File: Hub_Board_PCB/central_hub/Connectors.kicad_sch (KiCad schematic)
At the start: 12 parts, among them J3 Screw_Terminal_01x08, J4 Screw_Terminal_01x08, J5 CSP-USC16-TR, J6 Screw_Terminal_01x04, J6 Screw_Terminal_01x06, J8 Conn_01x02

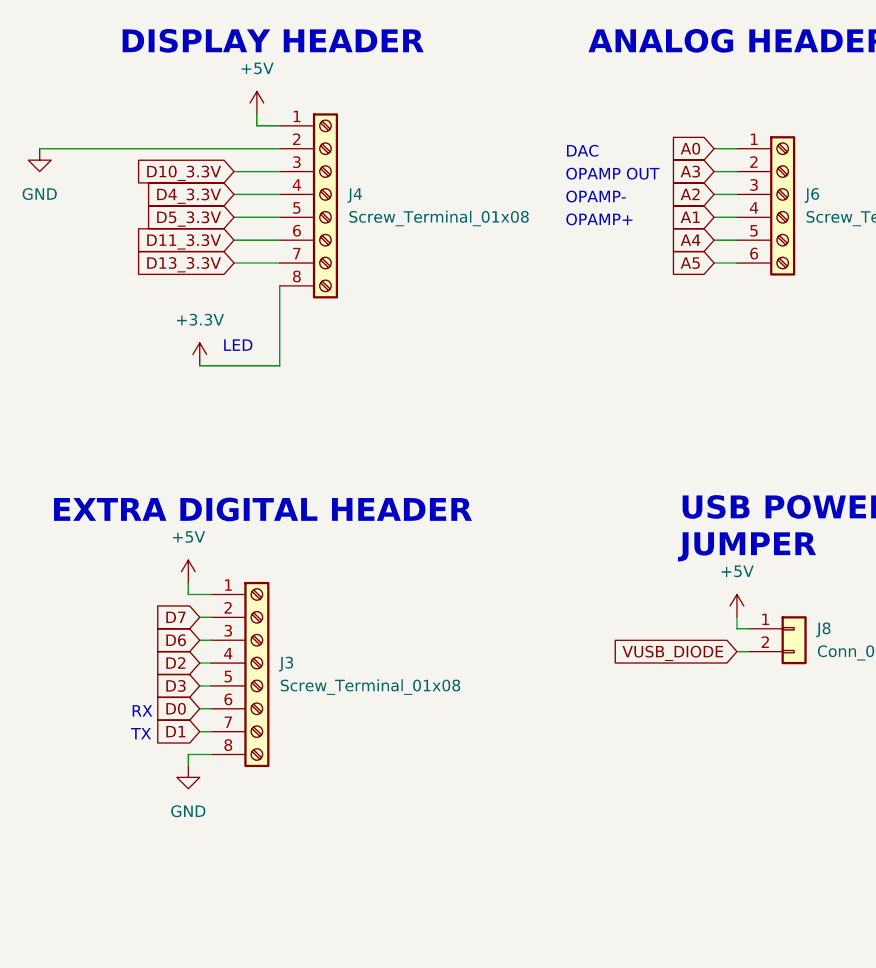
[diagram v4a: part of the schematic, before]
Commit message: Prelim layout + routing for hub PCB
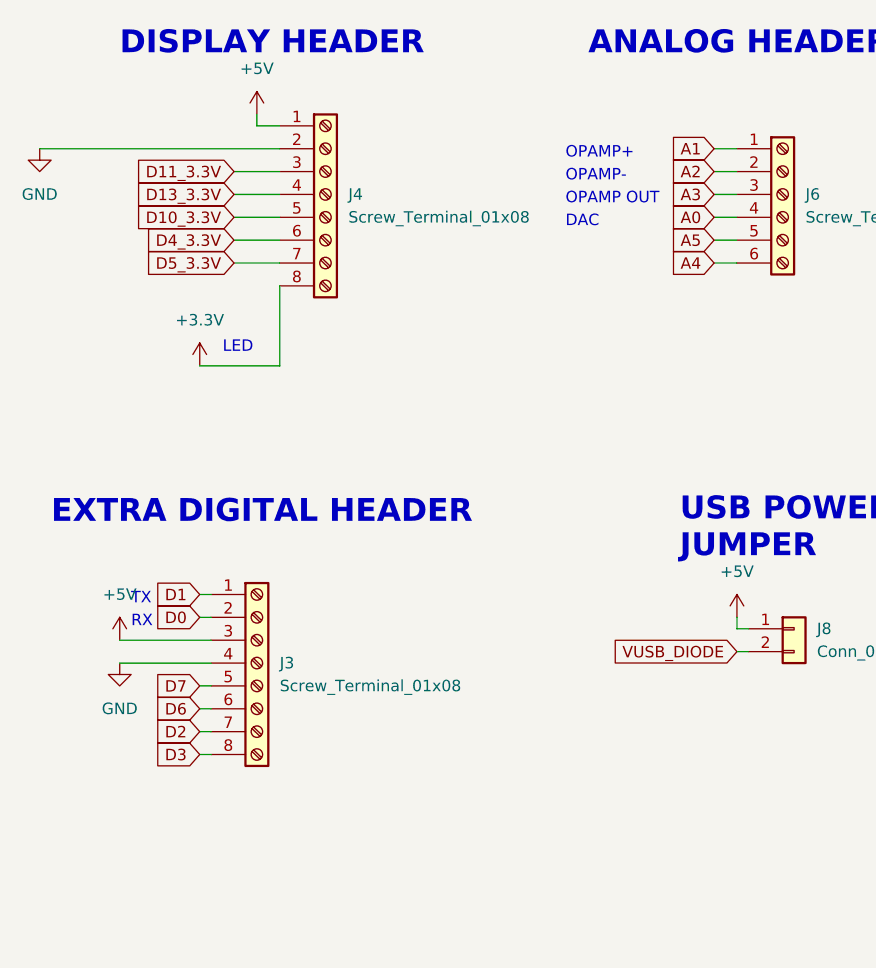
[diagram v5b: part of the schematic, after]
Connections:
- net +5V: now also J3.3 (Pin_3); no longer J3.1 (Pin_1)
- net A0: now also J6.4 (Pin_4); no longer J6.1 (Pin_1)
- net A1: now also J6.1 (Pin_1); no longer J6.4 (Pin_4)
- net A2: now also J6.2 (Pin_2); no longer J6.3 (Pin_3)
- net A3: now also J6.3 (Pin_3); no longer J6.2 (Pin_2)
- net A4: now also J6.6 (Pin_6); no longer J6.5 (Pin_5)
- net A5: now also J6.5 (Pin_5); no longer J6.6 (Pin_6)
- net D0: now also J3.2 (Pin_2); no longer J3.6 (Pin_6)
- net D1: now also J3.1 (Pin_1); no longer J3.7 (Pin_7)
- net D10_3.3V: now also J4.5 (Pin_5); no longer J4.3 (Pin_3)
- net D11_3.3V: now also J4.3 (Pin_3); no longer J4.6 (Pin_6)
- net D13_3.3V: now also J4.4 (Pin_4); no longer J4.7 (Pin_7)
- net D2: now also J3.7 (Pin_7); no longer J3.4 (Pin_4)
- net D3: now also J3.8 (Pin_8); no longer J3.5 (Pin_5)
- net D4_3.3V: now also J4.6 (Pin_6); no longer J4.4 (Pin_4)
- net D5_3.3V: now also J4.7 (Pin_7); no longer J4.5 (Pin_5)
- net D6: now also J3.6 (Pin_6); no longer J3.3 (Pin_3)
- net D7: now also J3.5 (Pin_5); no longer J3.2 (Pin_2)
- net GND: now also J3.4 (Pin_4); no longer J3.8 (Pin_8)

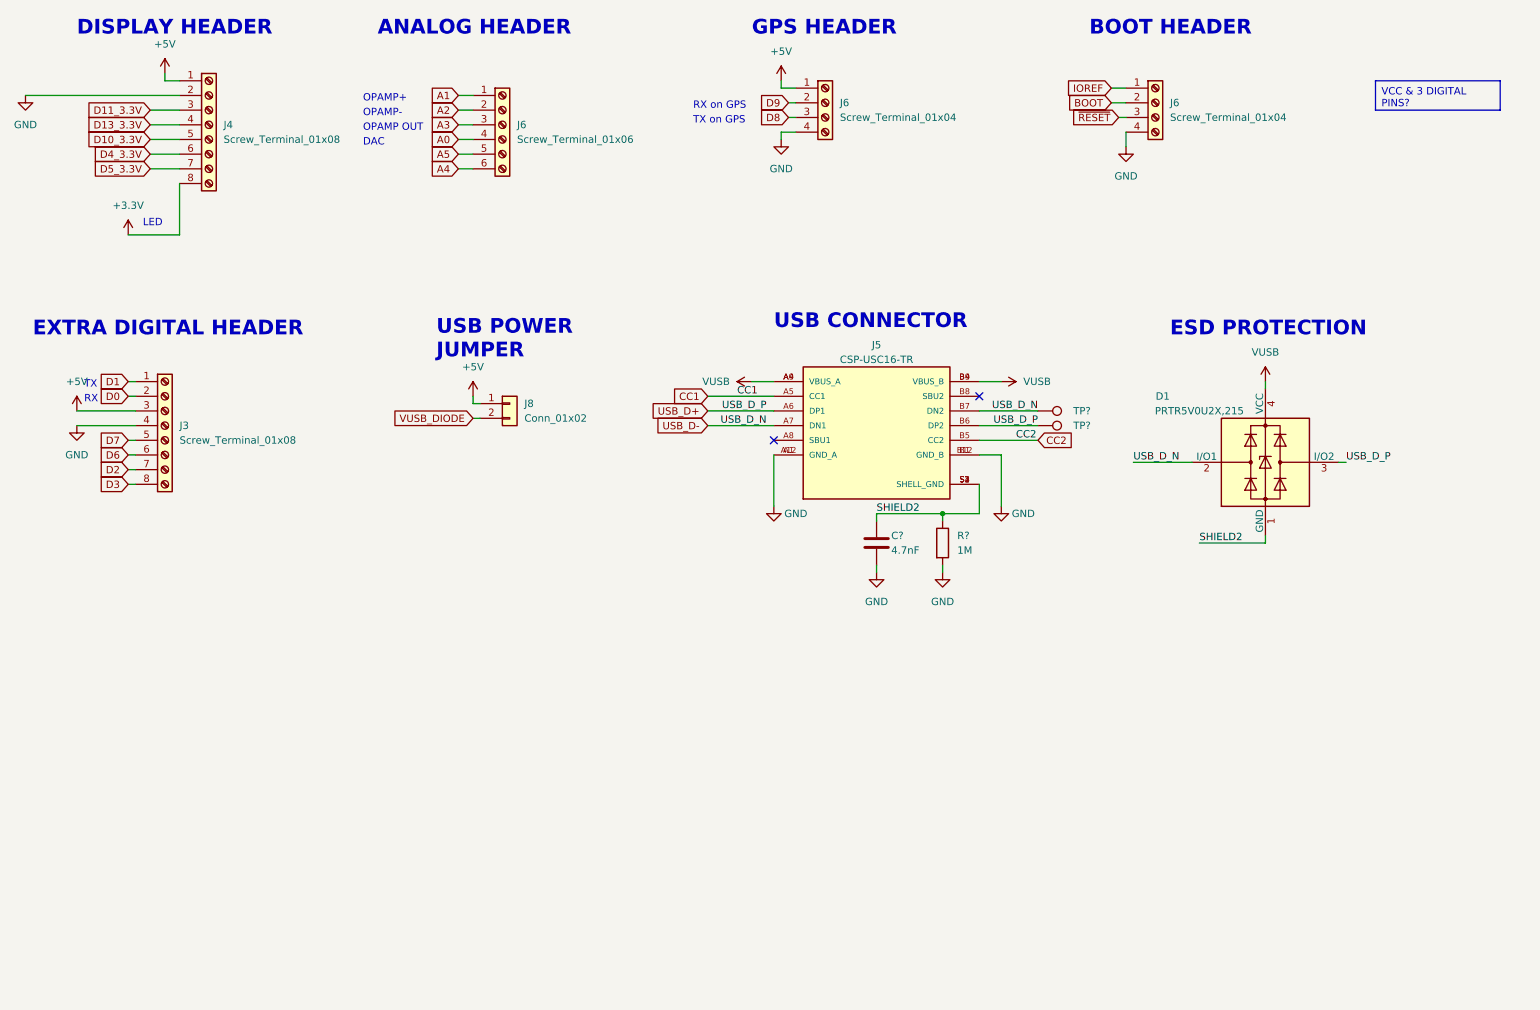
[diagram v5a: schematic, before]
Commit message: - fixed capacitor values on MCU sheet (both central hub and motor board) - added missing Accelerometer componenets - changed BOOT HEADER (both central hub and motor board) - set the Arduino "love" signal to NC - fixed overlapping pins on USB connector
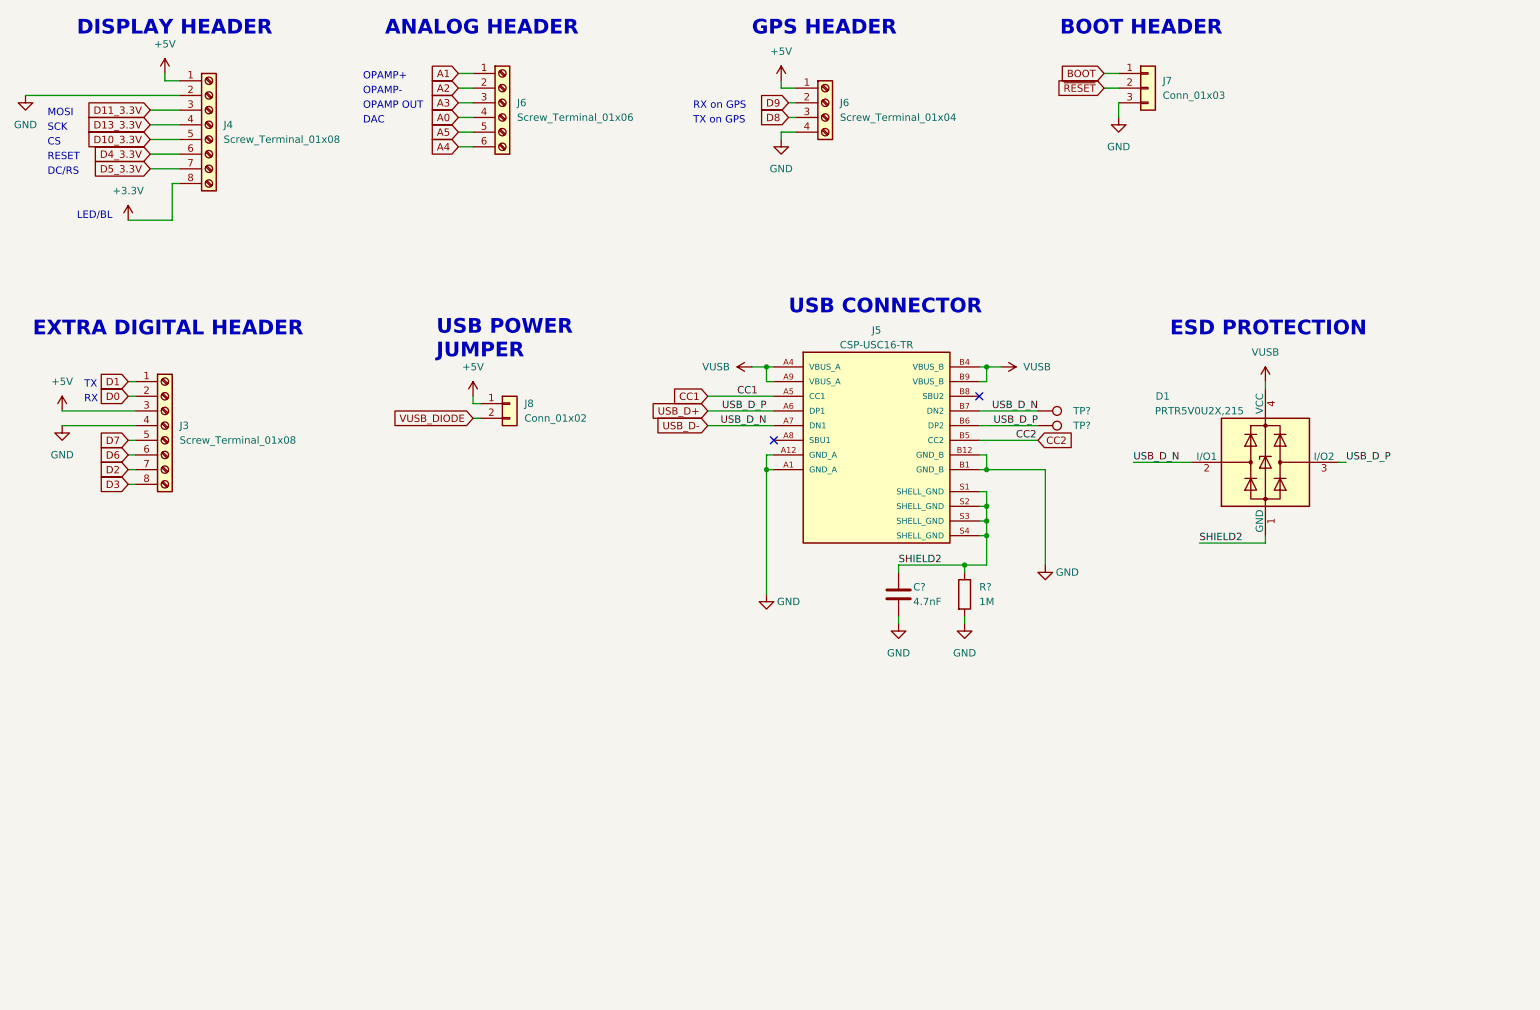
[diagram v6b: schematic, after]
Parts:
- removed J6: Screw_Terminal_01x04, Connector_PinHeader_2.54mm:PinHeader_1x04_P2.54mm_Vertical, symbol Connector:Screw_Terminal_01x04
- added J7: Conn_01x03, Connector_PinHeader_2.54mm:PinHeader_1x03_P2.54mm_Vertical, symbol Connector_Generic:Conn_01x03
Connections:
- net BOOT: now also J7.1 (Pin_1)
- net GND: now also J7.3 (Pin_3)
- net ~{RESET}: now also J7.2 (Pin_2)
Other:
- note added: "CS"
- note added: "DC/RS"
- note added: "LED/BL"
- note added: "MOSI"
- note added: "RESET"
- note added: "SCK"
- note removed: "LED"
- moved on the sheet: C?, J6, R?

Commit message: - added DNP caps for rotary encoder (debouncing)
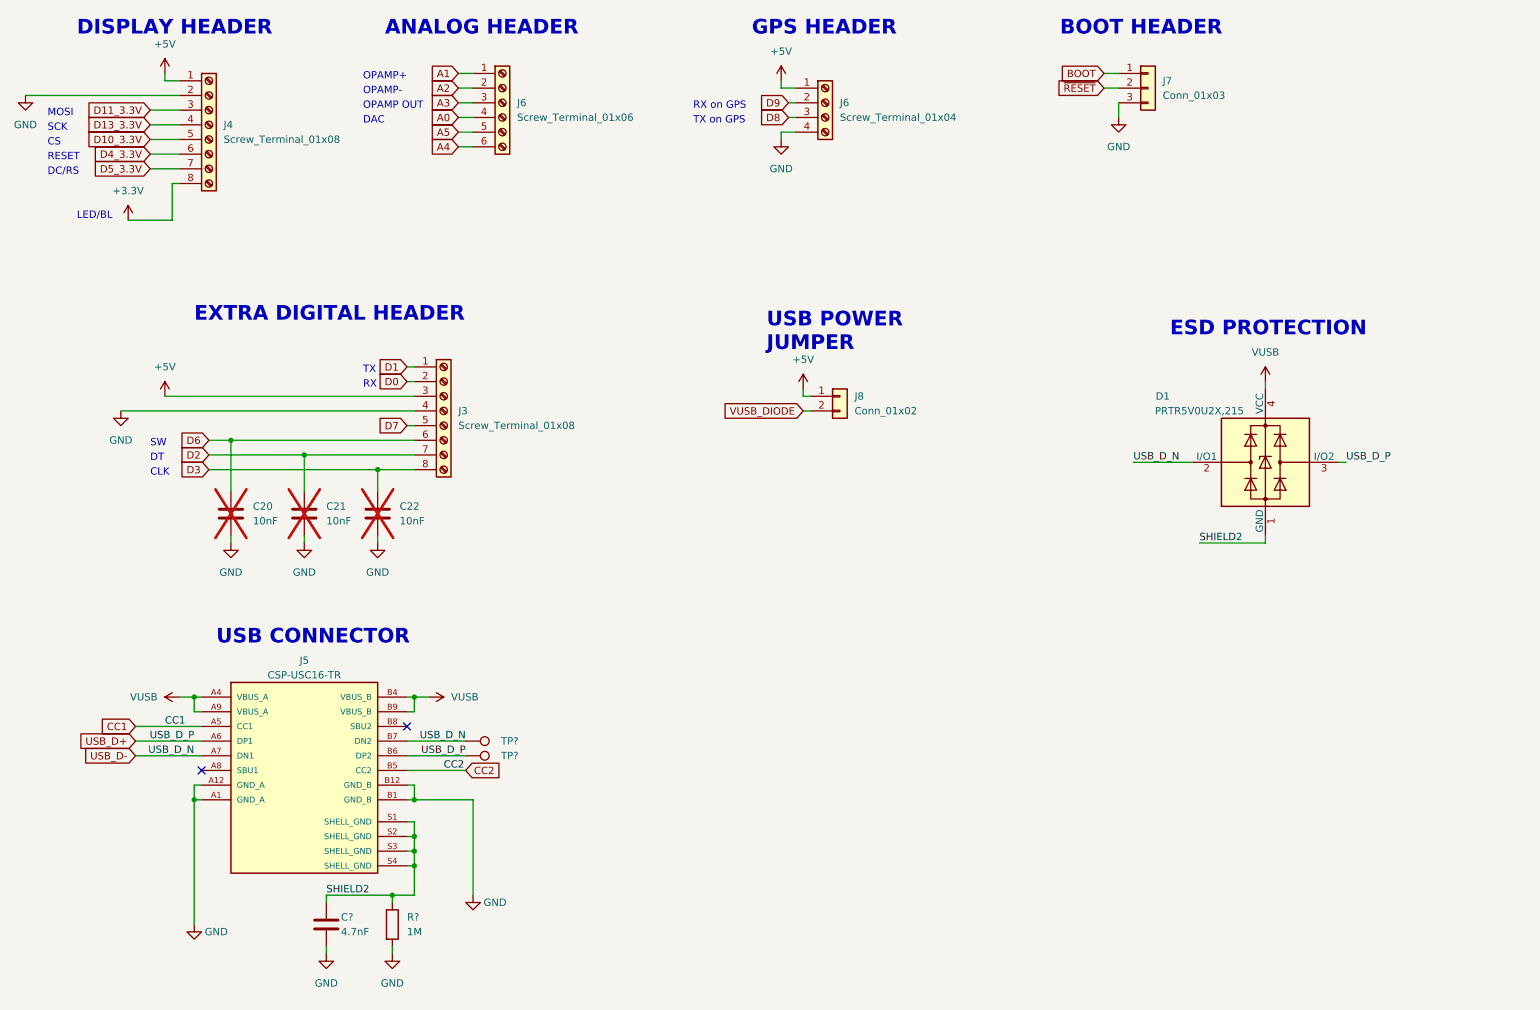
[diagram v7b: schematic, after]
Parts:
- added C20, C21, C22: 10nF, symbol Device:C
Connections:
- net D2: now also C21.1
- net D3: now also C22.1
- net D6: now also C20.1
- net GND: now also C20.2, C21.2, C22.2
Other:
- note added: "CLK"
- note added: "DT"
- note added: "SW"
- moved on the sheet: C?, J3, J5, J8, R?, TP?

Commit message: Schematic changes before sending to kim
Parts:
- removed J6: Screw_Terminal_01x06, Connector_PinHeader_2.54mm:PinHeader_1x06_P2.54mm_Vertical, symbol Connector:Screw_Terminal_01x06
- added J6: Screw_Terminal_01x04, Connector_PinHeader_2.54mm:PinHeader_1x04_P2.54mm_Vertical, symbol Connector:Screw_Terminal_01x04
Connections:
- net A0: now also J6.4
- net A1: now also J6.1
- net A2: now also J6.2
- net A3: now also J6.3
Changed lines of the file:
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@@
-    (stroke (width 0) (type default))
-  )
-  (wire (pts (xy 92.71 43.18) (xy 95.25 43.18))
     (stroke (width 0) (type default))
   )
@@
   )
   (wire (pts (xy 43.18 49.53) (xy 44.45 49.53))
-    (stroke (width 0) (type default))
-  )
-  (wire (pts (xy 92.71 40.64) (xy 95.25 40.64))
     (stroke (width 0) (type default))
   )
@@
     (effects (font (size 1.27 1.27)) (justify right))
     (property "Intersheetrefs" "${INTERSHEET_REFS}" (at 87.4267 33.02 0)
-      (effects (font (size 1.27 1.27)) (justify right) hide)
-    )
-  )
-  (global_label "A5" (shape input) (at 92.71 40.64 180) (fields_autoplaced)
-    (effects (font (size 1.27 1.27)) (justify right))
-    (property "Intersheetrefs" "${INTERSHEET_REFS}" (at 87.4267 40.64 0)
       (effects (font (size 1.27 1.27)) (justify right) hide)
     )
@@
     (effects (font (size 1.27 1.27)) (justify right))
     (property "Intersheetrefs" "${INTERSHEET_REFS}" (at 87.4267 38.1 0)
-      (effects (font (size 1.27 1.27)) (justify right) hide)
-    )
-  )
-  (global_label "A4" (shape input) (at 92.71 43.18 180) (fields_autoplaced)
-    (effects (font (size 1.27 1.27)) (justify right))
-    (property "Intersheetrefs" "${INTERSHEET_REFS}" (at 87.4267 43.18 0)
       (effects (font (size 1.27 1.27)) (justify right) hide)
     )
@@
         (path "/4ad82a24-c992-45c9-b523-12e12bcd6ced/996060af-581e-425f-9e10-26ee39d5a960"
           (reference "J8") (unit 1)
+        )
+      )
+    )
+  )
+  (symbol (lib_id "Connector:Screw_Terminal_01x04") (at 100.33 33.02 0) (unit 1)
+    (in_bom yes) (on_board yes) (dnp no) (fields_autoplaced)
+    (property "Reference" "J6" (at 102.87 33.02 0)
+      (effects (font (size 1.27 1.27)) (justify left))
+    )
+    (property "Value" "Screw_Terminal_01x04" (at 102.87 35.56 0)
+      (effects (font (size 1.27 1.27)) (justify left))
+    )
+    (property "Footprint" "Connector_PinHeader_2.54mm:PinHeader_1x04_P2.54mm_Vertical" (at 100.33 33.02 0)
+      (effects (font (size 1.27 1.27)) hide)
+    )
+    (property "Datasheet" "~" (at 100.33 33.02 0)
+      (effects (font (size 1.27 1.27)) hide)
+    )
+    (pin "1")
+    (pin "2")
+    (pin "3")
+    (pin "4")
+    (instances
+      (project "central_hub"
+        (path "/0d9ec66e-0fbf-4d12-9b83-adf78971a00b"
+          (reference "J6") (unit 1)
+        )
+        (path "/0d9ec66e-0fbf-4d12-9b83-adf78971a00b/4fb60496-ee10-4e45-a75e-a49c2c8afc68"
+          (reference "J14") (unit 1)
+        )
+        (path "/0d9ec66e-0fbf-4d12-9b83-adf78971a00b/8e53aed1-21e6-440d-aae4-1b5509ec346a"
+          (reference "J6") (unit 1)
         )
       )
@@
         )
       )
-    )
-  )
-  (symbol (lib_id "Connector:Screw_Terminal_01x06") (at 100.33 35.56 0) (unit 1)
-    (in_bom yes) (on_board yes) (dnp no) (fields_autoplaced)
-    (property "Reference" "J6" (at 102.87 35.56 0)
-      (effects (font (size 1.27 1.27)) (justify left))
-    )
-    (property "Value" "Screw_Terminal_01x06" (at 102.87 38.1 0)
-      (effects (font (size 1.27 1.27)) (justify left))
-    )
-    (property "Footprint" "Connector_PinHeader_2.54mm:PinHeader_1x06_P2.54mm_Vertical" (at 100.33 35.56 0)
-      (effects (font (size 1.27 1.27)) hide)
-    )
-    (property "Datasheet" "~" (at 100.33 35.56 0)
-      (effects (font (size 1.27 1.27)) hide)
-    )
-    (pin "1")
-    (pin "2")
-    (pin "3")
-    (pin "4")
-    (pin "5")
-    (pin "6")
-    (instances
-      (project "central_hub"
-        (path "/0d9ec66e-0fbf-4d12-9b83-adf78971a00b/8e53aed1-21e6-440d-aae4-1b5509ec346a"
-          (reference "J6") (unit 1)
-        )
-      )
